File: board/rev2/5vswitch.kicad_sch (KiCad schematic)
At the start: 12 parts, among them Q1 Q_NMOS_DGS, U3 LTC4359-DCB, U4 TPS259472ARPWR

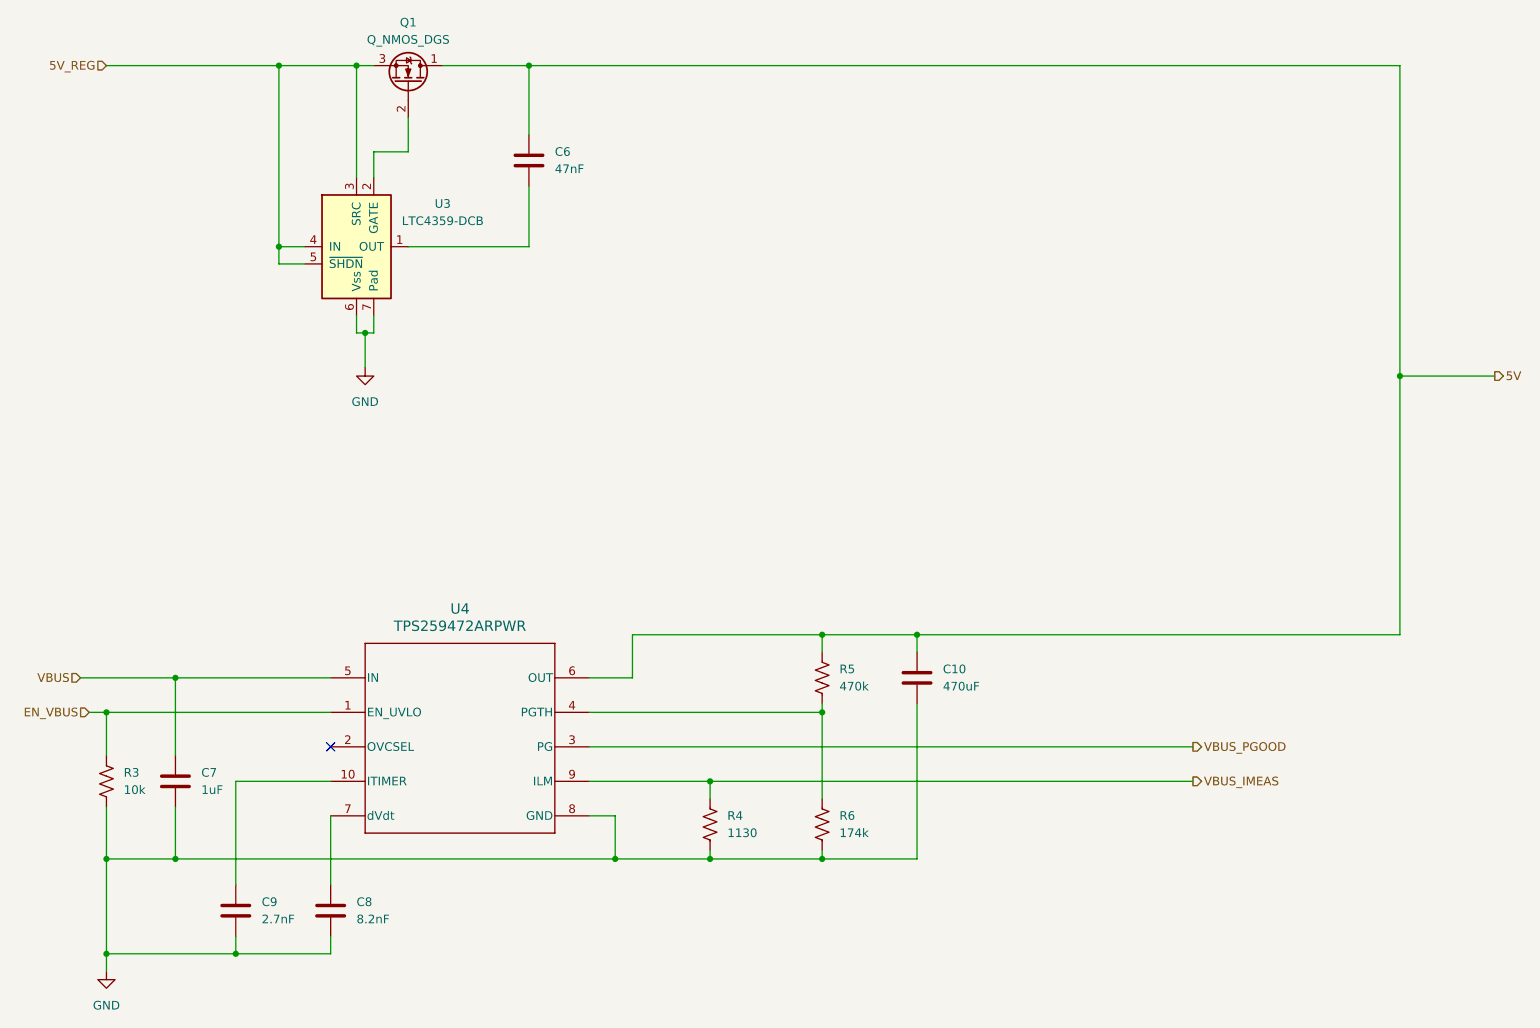
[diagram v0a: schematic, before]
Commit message: Finish most of power section of rev2 PCB
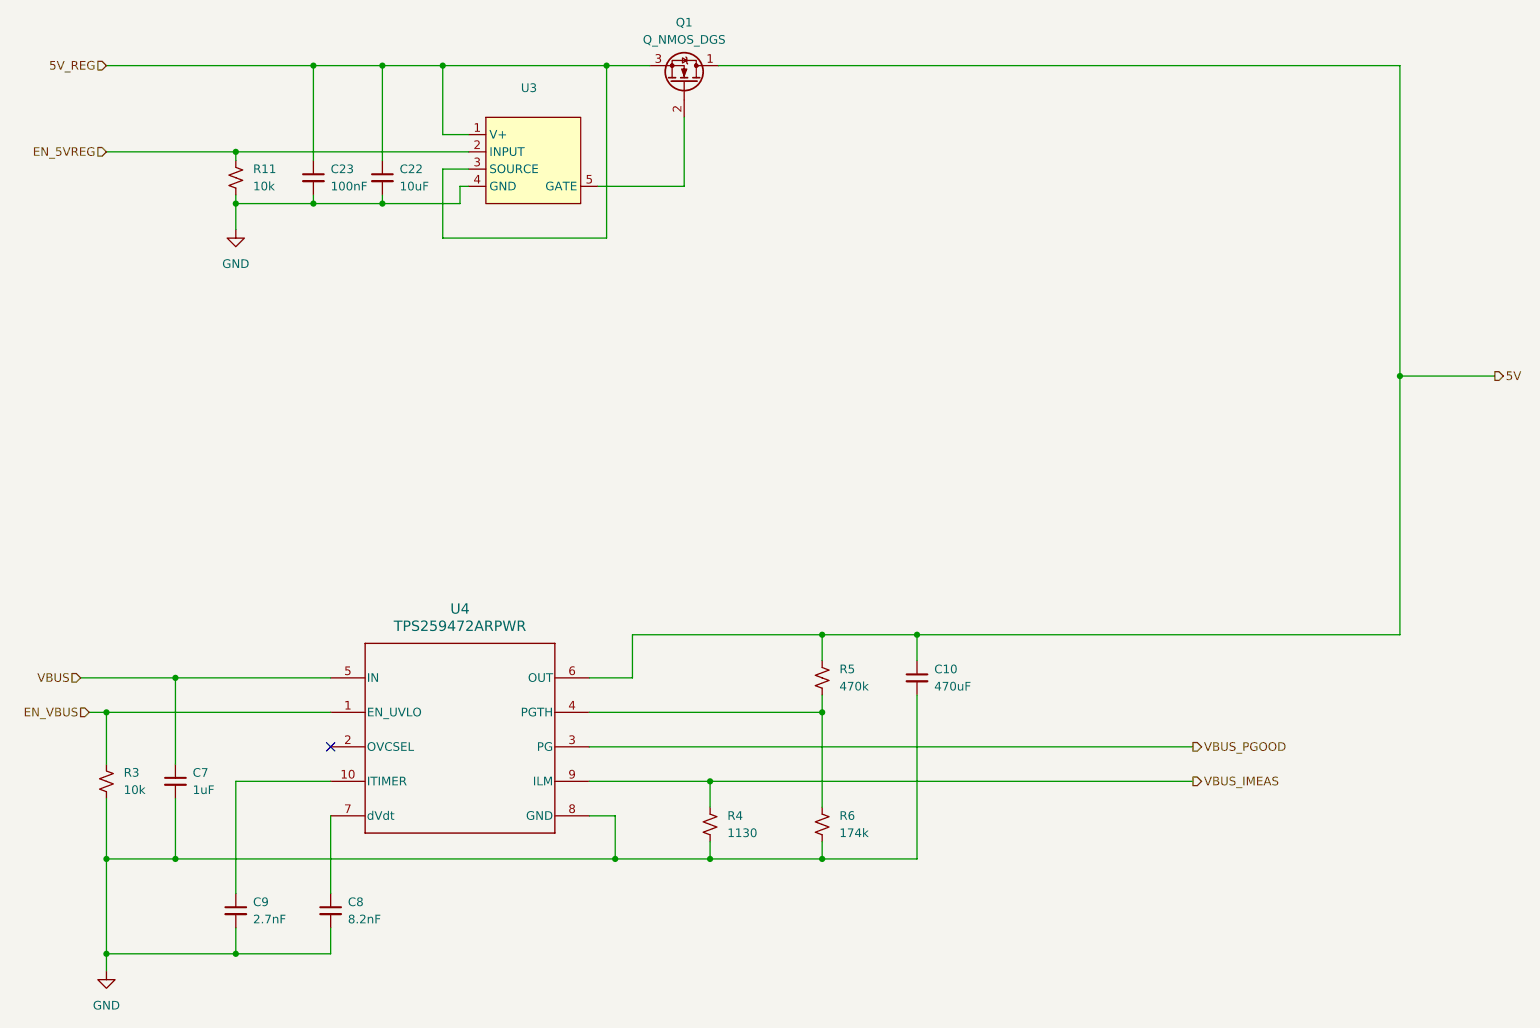
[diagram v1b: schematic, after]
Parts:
- removed C6: 47nF, symbol Device:C
- removed U3: LTC4359-DCB, Package_DFN_QFN:DFN-6-1EP_3x2mm_P0.5mm_EP1.65x1.35mm, symbol Power_Management:LTC4359-DCB
- added C22: 10uF, symbol Device:C_Small
- added C23: 100nF, symbol Device:C_Small
- added R11: 10k, symbol Device:R_Small_US
- added U3: ~, Package_SO:SOP-8_3.9x4.9mm_P1.27mm, symbol WUXI_GateDriver:MX5014S
- C10, C7, C8, C9: symbol Device:C -> Device:C_Small
- R3, R4, R5, R6: symbol Device:R_US -> Device:R_Small_US
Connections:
- net 5V_REG: now also C22.1, C23.1, U3.1 (V+), U3.3 (SOURCE)
- net GND: now also C22.2, C23.2, R11.2, U3.4 (GND)
- net at Q1.2 (G): now also U3.5 (GATE)
- new net EN_5VREG: R11.1, U3.2 (INPUT)

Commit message: More board stuff
(better clk routing, etc.)
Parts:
- removed C23: 100nF, symbol Device:C_Small
- removed U3: ~, Package_SO:SOP-8_3.9x4.9mm_P1.27mm, symbol WUXI_GateDriver:MX5014S
- added U3: LM5050-1, Package_TO_SOT_SMD:TSOT-23-6, symbol Power_Management:LM5050-1
- C22: value 10uF -> 100nF
- Q1: value Q_NMOS_DGS -> WSD40120DN56G
- R11: value 10k -> 100
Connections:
- net 5V: now also U3.6 (OUT)
- net 5V_REG: now also U3.4 (IN); no longer C22.1
- net EN_5VREG: now also U3.3 (OFF); no longer R11.1
- net GND: now also U3.2 (GND); no longer R11.2
- net VBUS: now also R11.1
- net at Q1.2 (G): now also U3.5 (GATE)
- new net: C22.1, R11.2, U3.1 (VS)
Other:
- moved on the sheet: Q1
